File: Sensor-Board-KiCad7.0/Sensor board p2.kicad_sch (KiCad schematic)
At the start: 62 parts, among them J10 9401-0-15-15-23-27-10-0, J12 9401-0-15-15-23-27-10-0, J13 9401-0-15-15-23-27-10-0, J14 9401-0-15-15-23-27-10-0, J15 9401-0-15-15-23-27-10-0, J16 9401-0-15-15-23-27-10-0, J17 9401-0-15-15-23-27-10-0, J18 9401-0-15-15-23-27-10-0, J19 9401-0-15-15-23-27-10-0, U14 PS1-NO2-50, U15 PS1-CO-1000, U16 LMV721, U17 LMV721, U18 LMV721, U19 PS1-SO2-50, U21 LMV721, U22 LMV721, U23 OPAMP, U24 BME680, U25 NAU7802_24-bit_ADC, U26 NAU7802_24-bit_ADC, U29 MMBFJ177LT1G, U30 MMBFJ177LT1G, U31 MMBFJ177LT1G

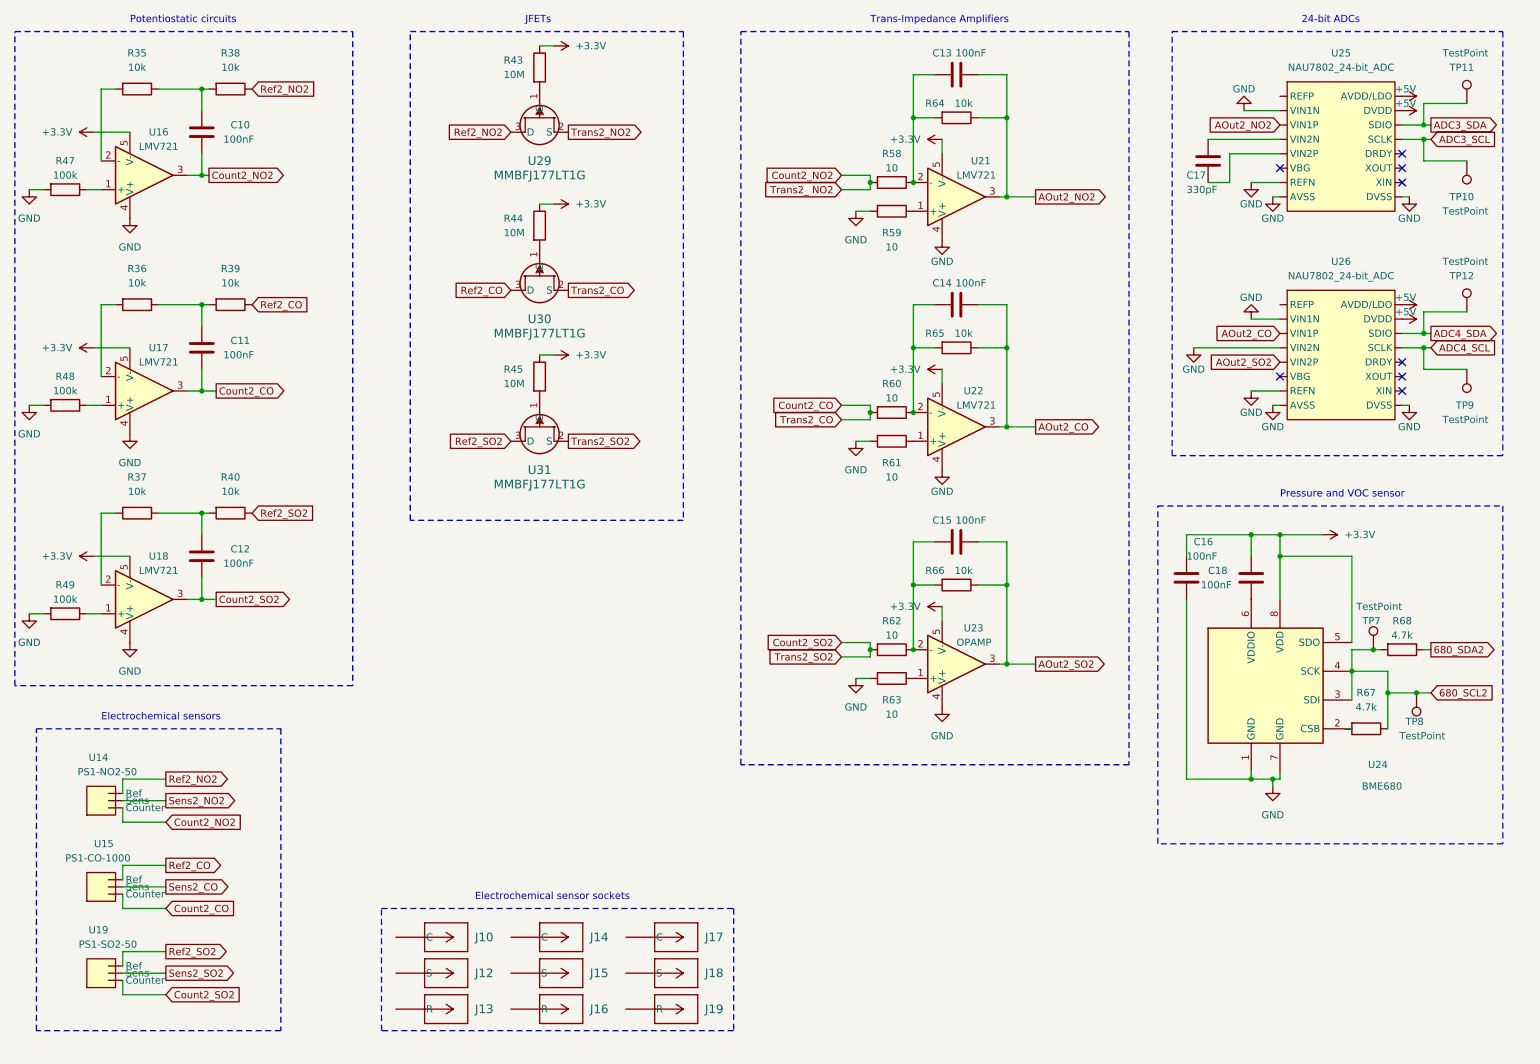
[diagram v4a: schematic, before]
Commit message: Final check
Added 10k resistors to + input of opamps. Added JFET symbol and footprint. Changed opamp from LMV721 to OPA386 to conform to 3-electrode design sheet. Fixed circuit for BME680. Added test points.
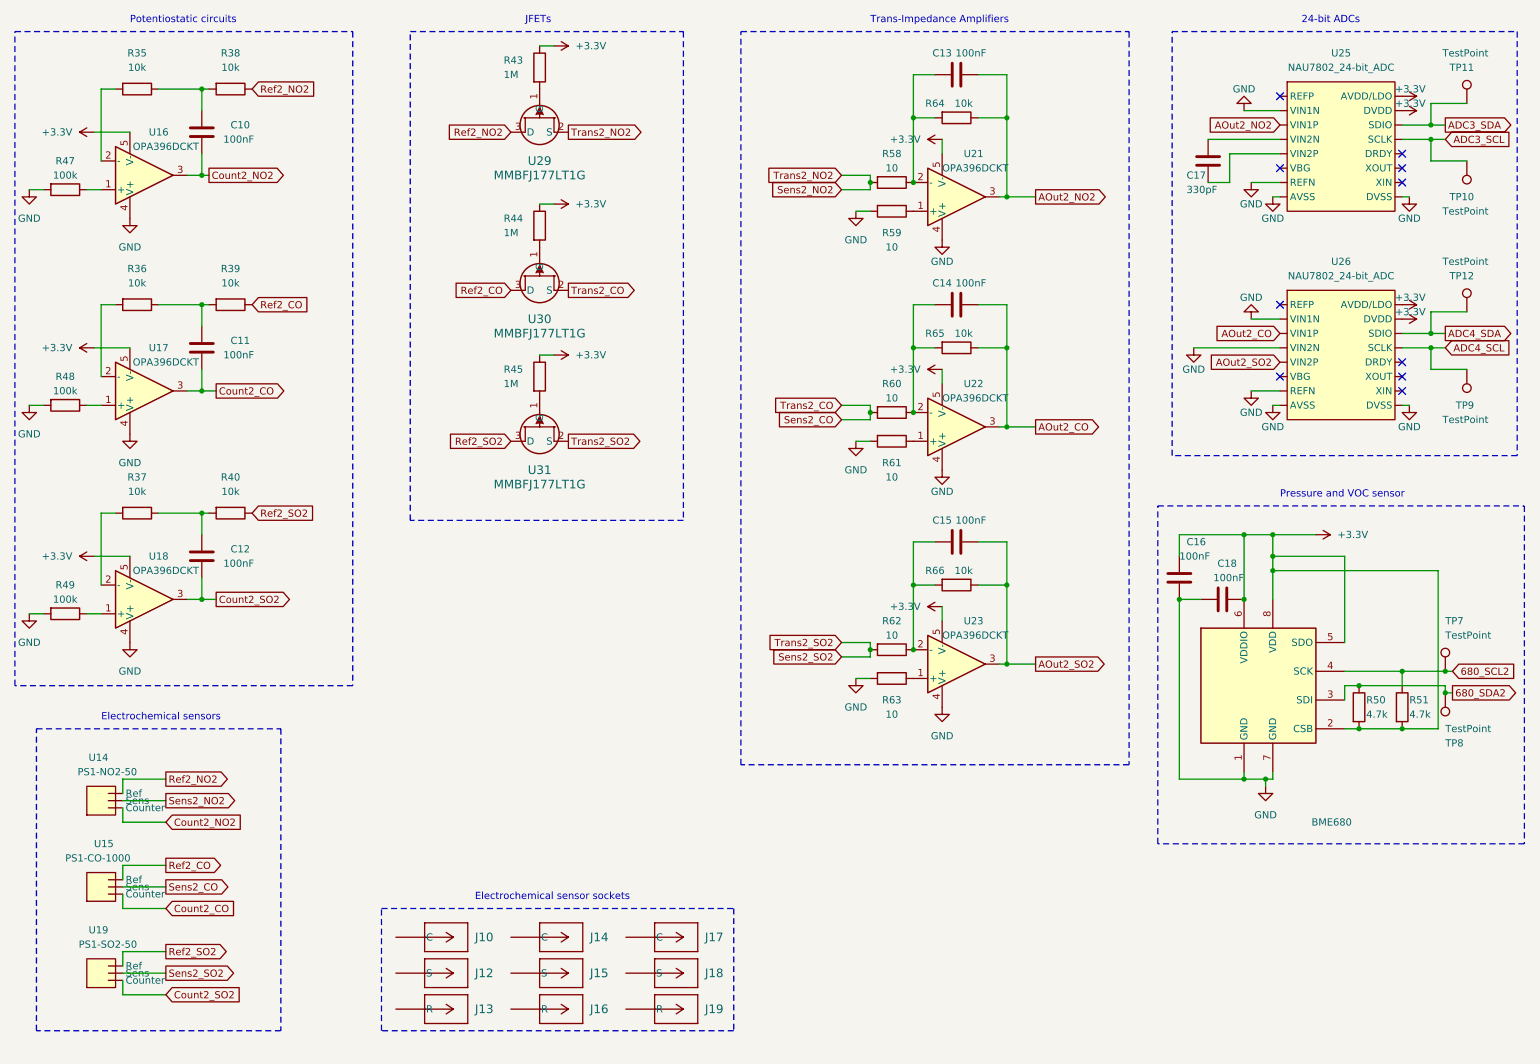
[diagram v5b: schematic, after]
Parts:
- removed R67, R68: 4.7k, symbol Device:R
- added R50, R51: 4.7k, symbol Device:R
- R43, R44, R45: value 10M -> 1M
- U16, U17, U18, U21, U22: value LMV721 -> OPA396DCKT
- U23: value OPAMP -> OPA396DCKT
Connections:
- net +5V is gone; now on net GND: U25. (XOUT), U26. (XOUT)
- net Trans2_NO2 is gone; now on net Sens2_NO2: U29.2 (S)
- net +3.3V: now also C18.2, U24.2 (CSB), U24.6 (VDDIO), U25. (XOUT), U26. (XOUT), R50.2, R51.2; no longer C18.1
- net 680_SCL2: now also R51.1; no longer TP8.1, U24.3 (SDI)
- net 680_SDA2: now also TP8.1, U24.3 (SDI), R50.1
- net Count2_CO: no longer R60.2, U30.2 (S)
- net Count2_NO2: no longer R58.2
- net Count2_SO2: no longer R62.2, U31.2 (S)
- net GND: now also C18.1
- net Sens2_CO: now also R60.2, U30.2 (S)
- net Sens2_NO2: now also R58.2
- net Sens2_SO2: now also R62.2, U31.2 (S)
- no-connect marks 8 -> 10

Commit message: Updated symbols + footprints
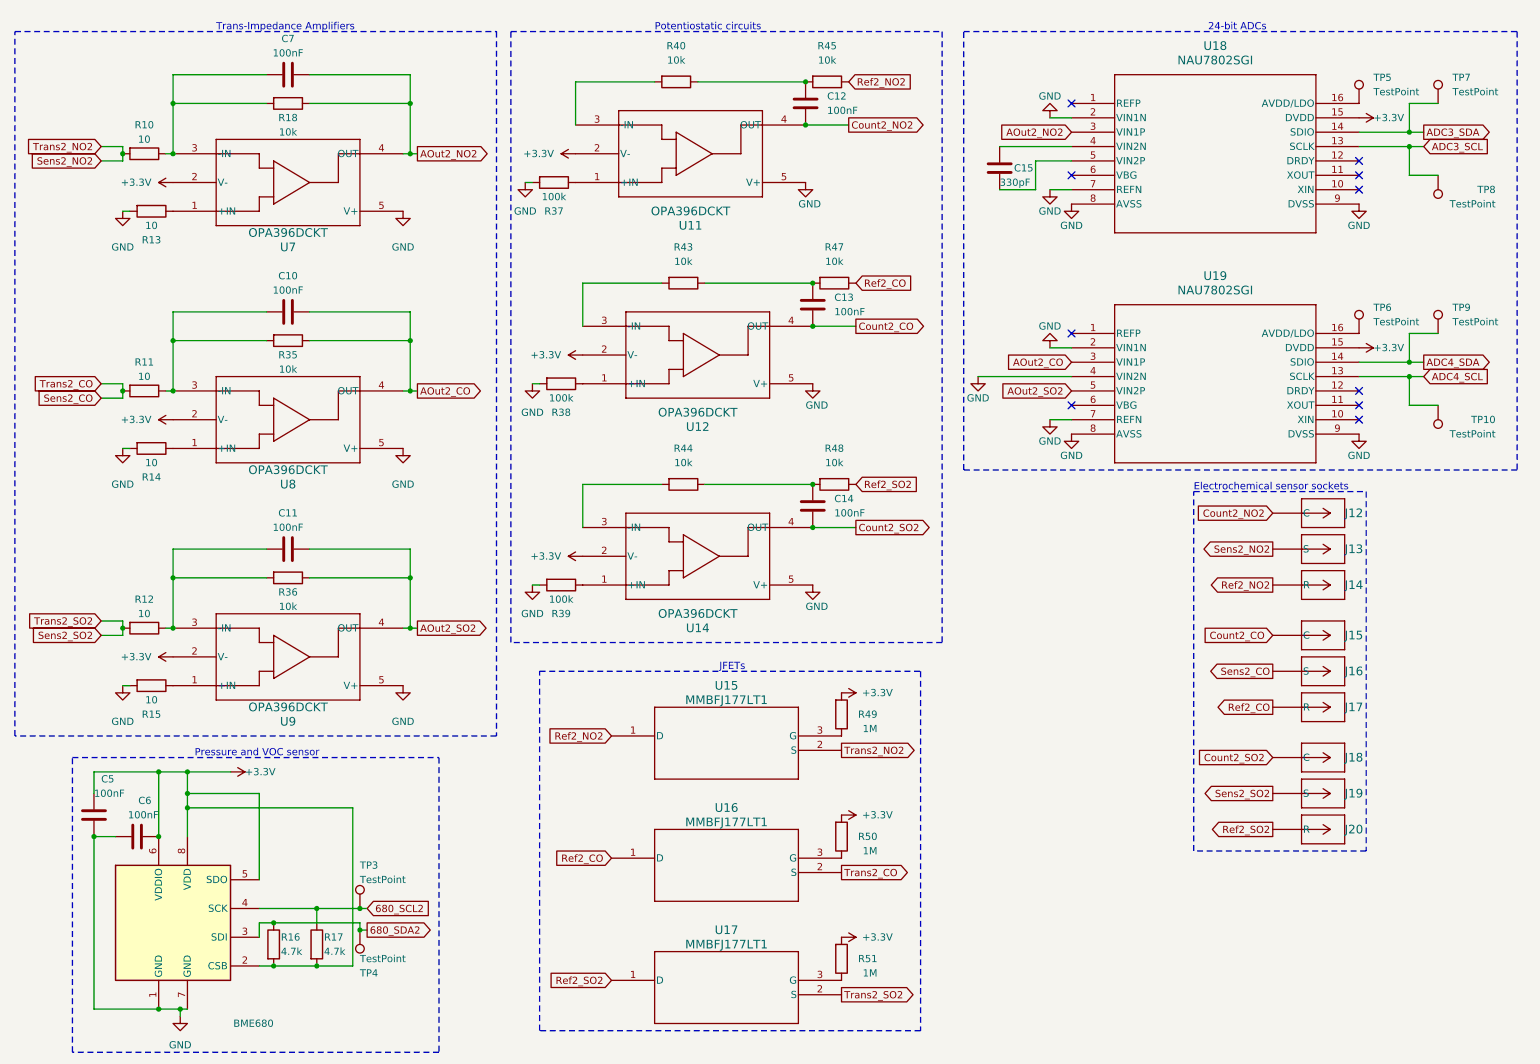
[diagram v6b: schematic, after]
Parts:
- removed C16, C18: 100nF, symbol Device:C
- removed C17: 330pF, symbol Device:C
- removed J10: 9401-0-15-15-23-27-10-0, CONN_0384-0-67-80-23-27-10-0_MIM, symbol EChem Socket:9401-0-15-15-23-27-10-0
- removed R58, R59, R60, R61, R62, R63: 10, symbol Device:R
- removed R64, R65, R66: 10k, symbol Device:R
- removed TP11, TP12: TestPoint, symbol Connector:TestPoint
- removed U14: PS1-NO2-50, symbol ElectrochemcialSensors:PS1-NO2-50
- removed U15: PS1-CO-1000, symbol ElectrochemcialSensors:PS1-CO-1000
- removed U16, U17, U18, U21, U22, U23: OPA396DCKT, symbol pspice:OPAMP
- removed U19: PS1-SO2-50, symbol ElectrochemcialSensors:PS1-SO2-50
- removed U24: BME680, Package_LGA:Bosch_LGA-8_3x3mm_P0.8mm_ClockwisePinNumbering, symbol Sensor:BME680
- removed U25, U26: NAU7802_24-bit_ADC, symbol ADCs:NAU7802_24-bit_ADC
- removed U29, U30, U31: MMBFJ177LT1G, SOT_77LT1G_ONS, symbol MMBFJ177LT1-D:MMBFJ177LT1G
- added C5, C6, C7: 100nF, symbol Device:C
- added J20: 9401-0-15-15-23-27-10-0, CONN_0384-0-67-80-23-27-10-0_MIM, symbol EChem Socket:9401-0-15-15-23-27-10-0
- added R10, R11, R12, R13, R14, R15: 10, symbol Device:R
- added R16, R17: 4.7k, symbol Device:R
- added R18: 10k, symbol Device:R
- added TP3, TP4, TP5, TP6: TestPoint, symbol Connector:TestPoint
- added U11, U12, U14, U7, U8, U9: OPA396DCKT, SC_96DCKT_TEX, symbol OPA396DCKT:OPA396DCKT
- added U15, U16, U17: MMBFJ177LT1, SOT-23-3_1P4X3P040_ONS, symbol MMBFJ177LT1G:MMBFJ177LT1
- added U18, U19: NAU7802SGI, SOI16_NAU7802SGI_NUV, symbol NAU7802:NAU7802SGI
- added U6: BME680, Package_LGA:Bosch_LGA-8_3x3mm_P0.8mm_ClockwisePinNumbering, symbol Sensor:BME680
- C15: value 100nF -> 330pF
- R37, R38, R39: value 10k -> 100k
- R43, R44, R45: value 1M -> 10k
- R47, R48: value 100k -> 10k
- R49: value 100k -> 1M
- R50, R51: value 4.7k -> 1M
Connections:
- net +3.3V: now also R49.2, C5.1, C6.2, R16.2, R17.2, U11.2 (V-), U12.2 (V-), U14.2 (V-), U18.15 (DVDD), U19.15 (DVDD), U6.2 (CSB), U6.5 (SDO), U6.6 (VDDIO), U6.8 (VDD), U7.2 (V-), U8.2 (V-), U9.2 (V-); no longer R43.1, R44.1, R45.1
- net 680_SCL2: now also R17.1, TP3.1, U6.4 (SCK); no longer R51.1, TP7.1
- net 680_SDA2: now also R16.1, TP4.1, U6.3 (SDI); no longer R50.1, TP8.1
- net ADC3_SCL: now also TP8.1, U18.13 (SCLK); no longer TP10.1
- net ADC3_SDA: now also TP7.1, U18.14 (SDIO)
- net ADC4_SCL: now also TP10.1, U19.13 (SCLK); no longer TP9.1
- net ADC4_SDA: now also TP9.1, U19.14 (SDIO)
- net AOut2_CO: now also C10.1, R35.1, U19.3 (VIN1P), U8.4 (OUT); no longer C14.1
- net AOut2_NO2: now also C7.1, R18.1, U18.3 (VIN1P), U7.4 (OUT); no longer C13.1
- net AOut2_SO2: now also C11.1, R36.1, U19.5 (VIN2P), U9.4 (OUT); no longer C15.1
- net Count2_CO: now also C13.2, J15. (C), U12.4 (OUT); no longer C11.2
- net Count2_NO2: now also C12.2, J12. (C), U11.4 (OUT); no longer C10.2
- net Count2_SO2: now also C14.2, J18. (C), U14.4 (OUT); no longer C12.2
- net GND: now also R37.2, R38.2, R39.2, C5.2, C6.1, R13.2, R14.2, R15.2, U11.5 (V+), U12.5 (V+), U14.5 (V+), U18.2 (VIN1N), U18.7 (REFN), U18.8 (AVSS), U18.9 (DVSS), U19.2 (VIN1N), U19.4 (VIN2N), U19.7 (REFN), U19.8 (AVSS), U19.9 (DVSS), U6.1 (GND), U6.7 (GND), U7.5 (V+), U8.5 (V+), U9.5 (V+); no longer R47.2, R48.2, R49.2
- net Ref2_CO: now also J17. (R), R47.1, U16.1 (D); no longer R39.1
- net Ref2_NO2: now also J14. (R), R45.1, U15.1 (D); no longer R38.1
- net Ref2_SO2: now also R48.1, J20. (R), U17.1 (D); no longer R40.1
- net Sens2_CO: now also J16. (S), R11.2, U16.2 (S)
- net Sens2_NO2: now also J13. (S), R10.2, U15.2 (S)
- net Sens2_SO2: now also J19. (S), R12.2, U17.2 (S)
- net at C15.2: now also U18.5 (VIN2P)
- net at R43.2: now also U12.3 (-IN)
- net at R36.2: now also C11.2, R12.1, U9.3 (-IN)
- net at R49.1: now also U15.3 (G)
- net at R44.2: now also U14.3 (-IN)
- net at R45.2: now also C12.1, R40.1
- net at R35.2: now also C10.2, R11.1, U8.3 (-IN)
- new net: R40.2, U11.3 (-IN)
- new net: TP6.1, U19.16 (AVDD/LDO)
- new net: R50.1, U16.3 (G)
- new net: R37.1, U11.1 (+IN)
- new net: R15.1, U9.1 (+IN)
- new net: R14.1, U8.1 (+IN)
- new net: R38.1, U12.1 (+IN)
- new net: C7.2, R10.1, R18.2, U7.3 (-IN)
- new net: R13.1, U7.1 (+IN)
- new net: C13.1, R43.1, R47.2
- new net: C15.1, U18.4 (VIN2N)
- new net: R51.1, U17.3 (G)
- new net: R39.1, U14.1 (+IN)
- new net: TP5.1, U18.16 (AVDD/LDO)
- new net: C14.1, R44.1, R48.2
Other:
- note removed: "Electrochemical sensors"

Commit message: Fixed a bunch of errors
Updated OPA396 symbol + footprints
Updated NAU7802 symbol + footprints
Updated MMBFJ177LT1 symbol + footprints
Updated EChem socket symbol + footprints
Updated I2C connector symbol + footprints
Fixed connection issues with EChem sockets
Removed net labels from EChem sockets
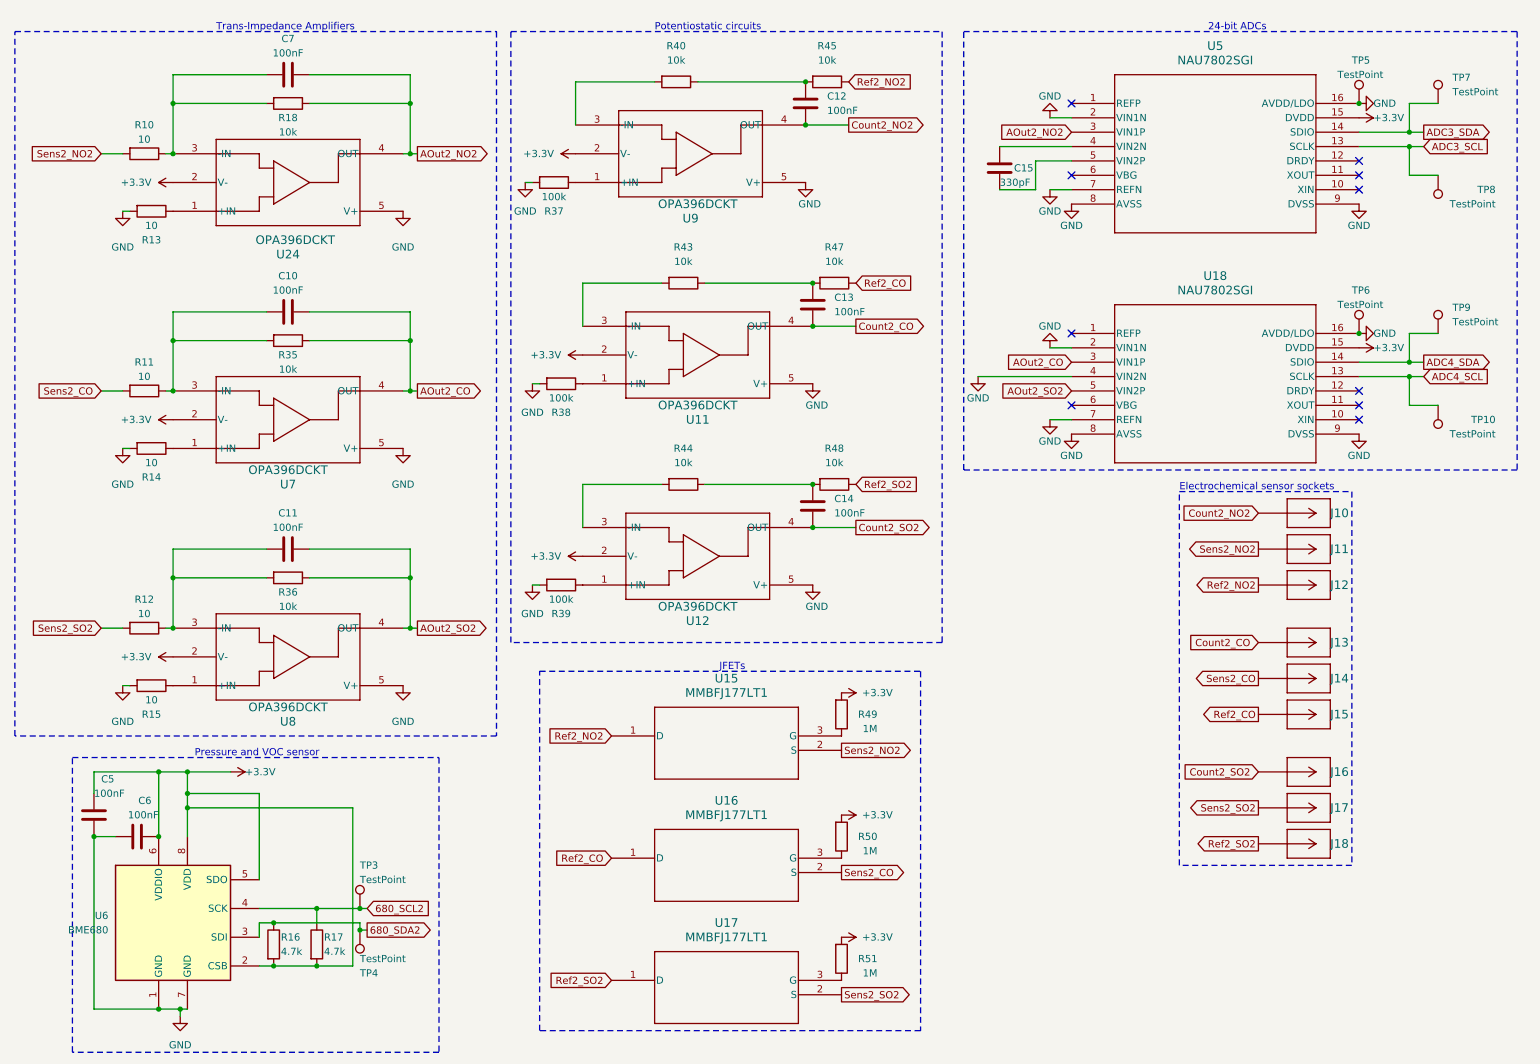
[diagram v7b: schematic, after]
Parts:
- removed J12, J13, J14, J15, J16, J17, J18, J19, J20: 9401-0-15-15-23-27-10-0, CONN_0384-0-67-80-23-27-10-0_MIM, symbol EChem Socket:9401-0-15-15-23-27-10-0
- removed U14: OPA396DCKT, SC_96DCKT_TEX, symbol OPA396DCKT:OPA396DCKT
- removed U19: NAU7802SGI, SOI16_NAU7802SGI_NUV, symbol NAU7802:NAU7802SGI
- added J10, J11, J12, J13, J14, J15, J16, J17, J18: 9401-0-15-15-23-27-10-0, CONN_0384-0-67-80-23-27-10-0_MIM, symbol EChem socket:9401-0-15-15-23-27-10-0
- added U24: OPA396DCKT, SC_96DCKT_TEX, symbol OPA396DCKT:OPA396DCKT
- added U5: NAU7802SGI, SOI16_NAU7802SGI_NUV, symbol NAU7802:NAU7802SGI
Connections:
- net +3.3V: now also U24.2 (V-), U5.15 (DVDD)
- net ADC3_SCL: now also U5.13 (SCLK); no longer U18.13 (SCLK)
- net ADC3_SDA: now also U5.14 (SDIO); no longer U18.14 (SDIO)
- net ADC4_SCL: now also U18.13 (SCLK)
- net ADC4_SDA: now also U18.14 (SDIO)
- net AOut2_CO: now also U18.3 (VIN1P), U7.4 (OUT); no longer U8.4 (OUT)
- net AOut2_NO2: now also U24.4 (OUT), U5.3 (VIN1P); no longer U18.3 (VIN1P), U7.4 (OUT)
- net AOut2_SO2: now also U18.5 (VIN2P), U8.4 (OUT); no longer U9.4 (OUT)
- net Count2_CO: now also U11.4 (OUT), J13.; no longer U12.4 (OUT)
- net Count2_NO2: now also U9.4 (OUT), J10.; no longer U11.4 (OUT)
- net Count2_SO2: now also U12.4 (OUT), J16.
- net GND: now also TP5.1, TP6.1, U18.16 (AVDD/LDO), U18.4 (VIN2N), U24.5 (V+), U5.16 (AVDD/LDO), U5.2 (VIN1N), U5.7 (REFN), U5.8 (AVSS), U5.9 (DVSS)
- net Ref2_CO: now also J15.
- net Ref2_NO2: now also J12.
- net Ref2_SO2: now also J18.
- net Sens2_CO: now also J14.
- net Sens2_NO2: now also J11.
- net Sens2_SO2: now also J17.
- net at R40.2: now also U9.3 (-IN); no longer U11.3 (-IN)
- net at C11.2, R12.1, R36.2: now also U8.3 (-IN); no longer U9.3 (-IN)
- net at R37.1: now also U9.1 (+IN); no longer U11.1 (+IN)
- net at R15.1: now also U8.1 (+IN); no longer U9.1 (+IN)
- net at R14.1: now also U7.1 (+IN); no longer U8.1 (+IN)
- net at R38.1: now also U11.1 (+IN); no longer U12.1 (+IN)
- net at C7.2, R10.1, R18.2: now also U24.3 (-IN); no longer U7.3 (-IN)
- net at R13.1: now also U24.1 (+IN); no longer U7.1 (+IN)
- net at R43.2: now also U11.3 (-IN); no longer U12.3 (-IN)
- net at C15.1: now also U5.4 (VIN2N); no longer U18.4 (VIN2N)
- net at C15.2: now also U5.5 (VIN2P); no longer U18.5 (VIN2P)
- net at C10.2, R11.1, R35.2: now also U7.3 (-IN); no longer U8.3 (-IN)
- net at R39.1: now also U12.1 (+IN)
- net at R44.2: now also U12.3 (-IN)

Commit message: Final check of schematic
Double-checked schematic for compliance to datasheets and design requirements. Assigned footprints to all resistors and capacitors
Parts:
- C10, C11, C12, C13, C14, C15, C5, C6, C7: footprint (none) -> Capacitor_SMD:C_0603_1608Metric
- J10, J11, J12, J13, J14, J15, J16, J17, J18: footprint CONN_0384-0-67-80-23-27-10-0_MIM -> EChem socket:CONN_0384-0-67-80-23-27-10-0_MIM
- R10, R11, R12, R13, R14, R15, R16, R17, R18, R35, R36, R40, R43, R44, R45, R47, R48, R49, R50, R51: footprint (none) -> Resistor_SMD:R_0603_1608Metric
- R37, R38, R39: value 100k -> 10k; footprint (none) -> Resistor_SMD:R_0603_1608Metric
- TP10, TP3, TP4, TP5, TP6, TP7, TP8, TP9: footprint (none) -> TestPoint:TestPoint_Pad_D1.5mm
- U11, U12, U24, U7, U8, U9: footprint SC_96DCKT_TEX -> OPA396DCKT:SC_96DCKT_TEX
- U15, U16, U17: footprint SOT-23-3_1P4X3P040_ONS -> MMBFJ177LT1G:SOT-23-3_1P4X3P040_ONS
- U18, U5: footprint SOI16_NAU7802SGI_NUV -> NAU7802:SOI16_NAU7802SGI_NUV
